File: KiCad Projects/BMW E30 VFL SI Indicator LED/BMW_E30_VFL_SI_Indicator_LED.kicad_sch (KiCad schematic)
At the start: 15 parts, among them J1 Conn_01x13_Socket

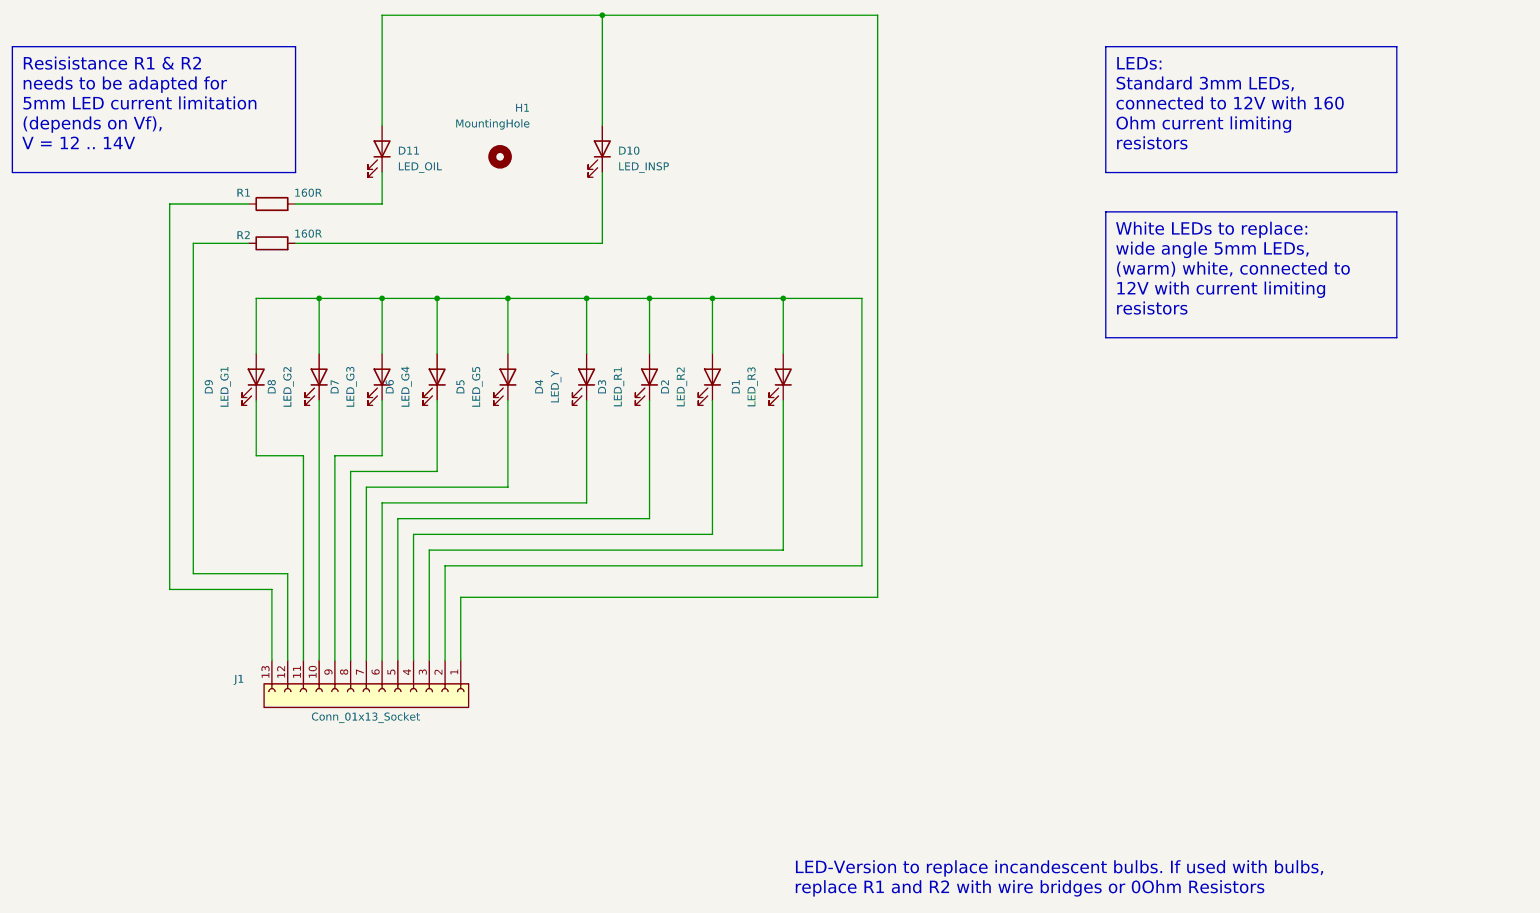
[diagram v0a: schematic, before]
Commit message: Updated resistor values
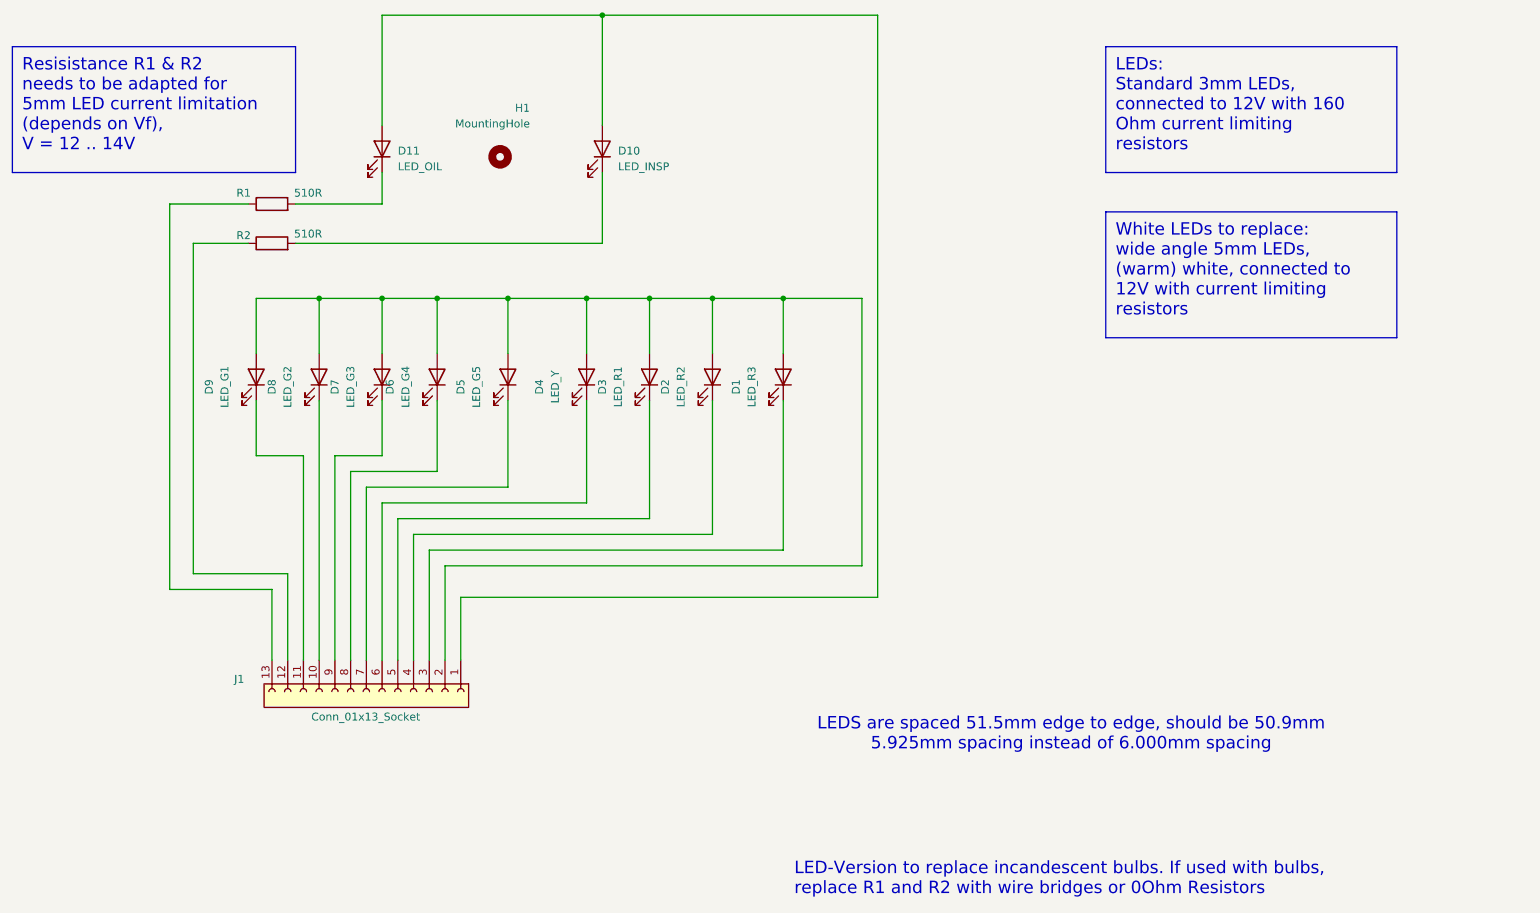
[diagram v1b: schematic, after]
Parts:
- R1, R2: value 160R -> 510R
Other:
- note added: "LEDS are spaced 51.5mm edge to edge, should be 50.9mm 5.925mm spacing instead of 6.000mm spacing"
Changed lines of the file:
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@@
+		)
+	)
+	(text "LEDS are spaced 51.5mm edge to edge, should be 50.9mm\n5.925mm spacing instead of 6.000mm spacing"
+		(exclude_from_sim no)
+		(at 225.552 150.368 0)
+		(effects
+			(font
+				(size 2 2)
+			)
 		)
 	)
@@
 			)
 		)
-		(property "Value" "160R"
+		(property "Value" "510R"
 			(at 102.362 69.596 90)
 			(effects
@@
 			)
 		)
-		(property "Value" "160R"
+		(property "Value" "510R"
 			(at 102.362 62.992 90)
 			(effects

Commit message: Increase mounting hole diameter to 6.5mm
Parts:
- H1: footprint MountingHole:MountingHole_5.5mm -> MountingHole:MountingHole_6.5mm
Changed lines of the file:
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@@
 			)
 		)
-		(property "Footprint" "MountingHole:MountingHole_5.5mm"
+		(property "Footprint" "MountingHole:MountingHole_6.5mm"
 			(at 133.35 57.15 0)
 			(effects
